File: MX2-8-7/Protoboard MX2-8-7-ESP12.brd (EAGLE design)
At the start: 64.4 x 71.2 mm, 146 parts, among them J1 DCJ0202

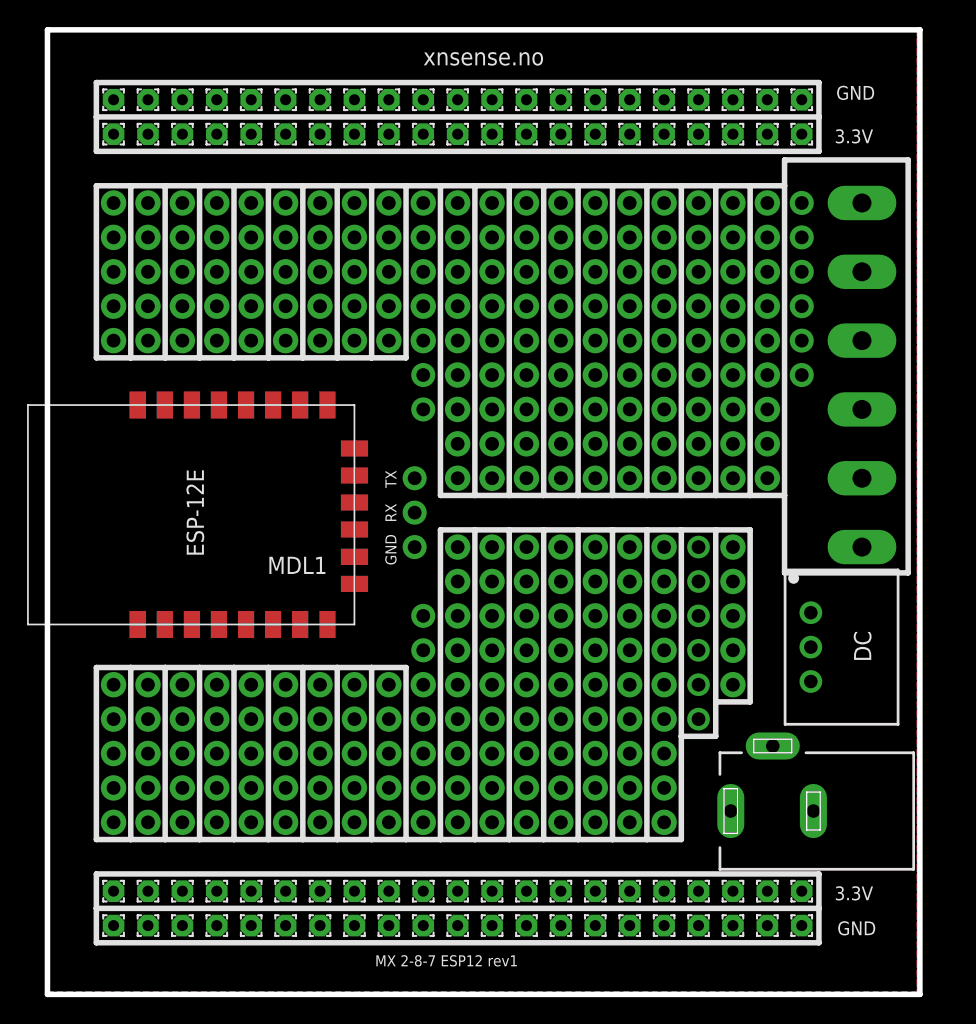
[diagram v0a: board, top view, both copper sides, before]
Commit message: Change usb connector
Change to correct usb connecter and moved esp8266 bit more onto the
board.
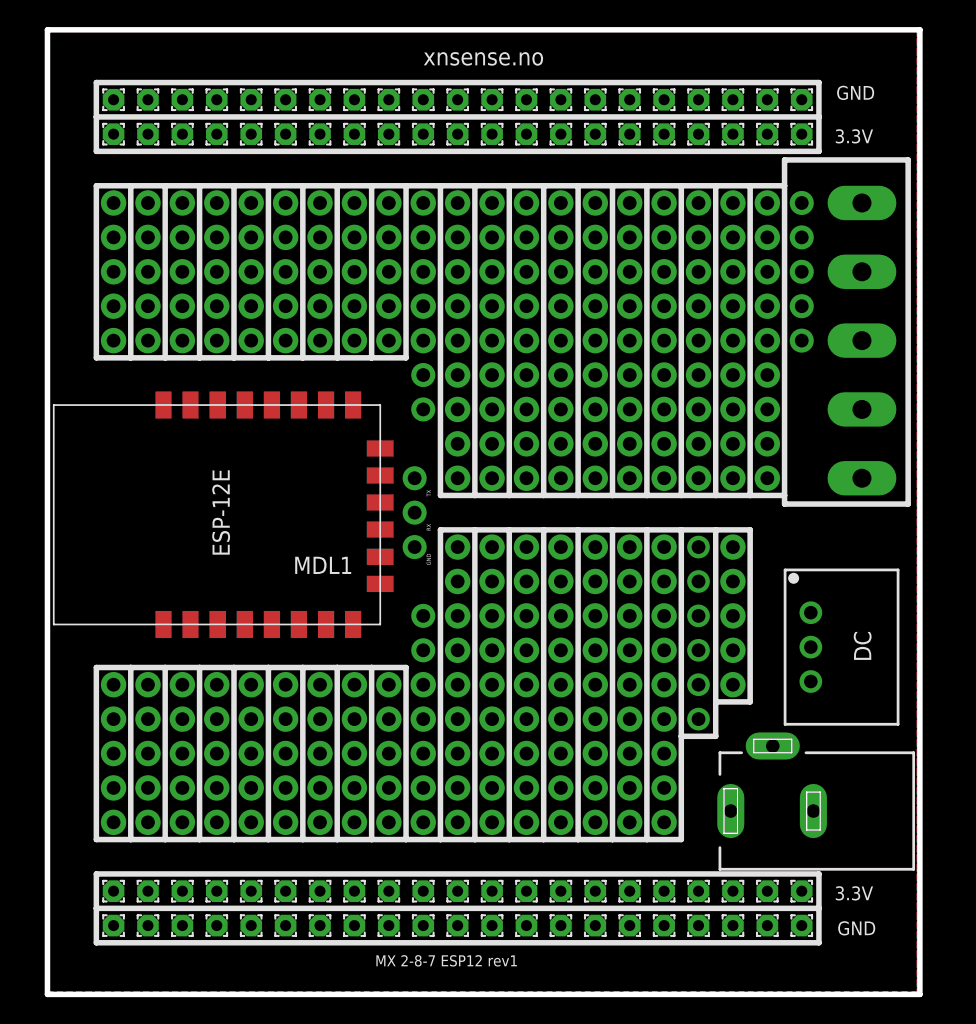
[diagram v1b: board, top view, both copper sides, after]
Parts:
- removed JP11: (no value), adafruit:1X01-CLEANBIG
- removed JP17: (no value), adafruit:1X1-BIGPOGO
- moved MDL1 1.91 mm to (14.6, 34.9)
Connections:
- removed net N$45: JP11.1, JP17.P$1

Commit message: Update esp component and usb
test
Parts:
- removed J1: DCJ0202, con-jack:DCJ0202
- removed MDL1: (no value), ESP8266-ESP12E:ESP8266-ESP12E
- added U2: (no value), SparkFun-PowerIC:SOT23-5
- added X1: ESP-12E, microbuilder:ESP-12E
- added X2: (no value), microbuilder:4UCONN_20329_V2
- moved DC 6.63 mm to (58.5, 19.3), turned to 180 degrees
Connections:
- new net N$45: TX.1, X1.15
- net GND: now also U2.2, X1.9; no longer J1.2, J1.3, MDL1.9
- net N$1: now also X1.14; no longer MDL1.14
- net N$22: now also X1.1; no longer MDL1.1
- net N$23: now also X1.2; no longer MDL1.2
- net N$24: now also X1.3; no longer MDL1.3
- net N$25: now also X1.4; no longer MDL1.4
- net N$26: now also X1.5; no longer MDL1.5
- net N$27: now also X1.6; no longer MDL1.6
- net N$28: now also X1.7; no longer MDL1.7
- net N$3: now also X1.13; no longer MDL1.13
- net N$4: now also X1.12; no longer MDL1.12
- net N$46: now also X1.16; no longer MDL1.15
- net N$47: now also X2.BASE@1, X2.BASE@2, X2.GND, X2.SPRT@1, X2.SPRT@2, X2.SPRT@3, X2.SPRT@4; no longer MDL1.16, TX.1
- net N$5: now also X1.11; no longer MDL1.11
- net N$6: now also X1.10; no longer MDL1.10
- net VCC: now also U2.1, U2.3, X2.VBUS; no longer J1.1
- net VDD: now also U2.5, X1.8; no longer MDL1.8

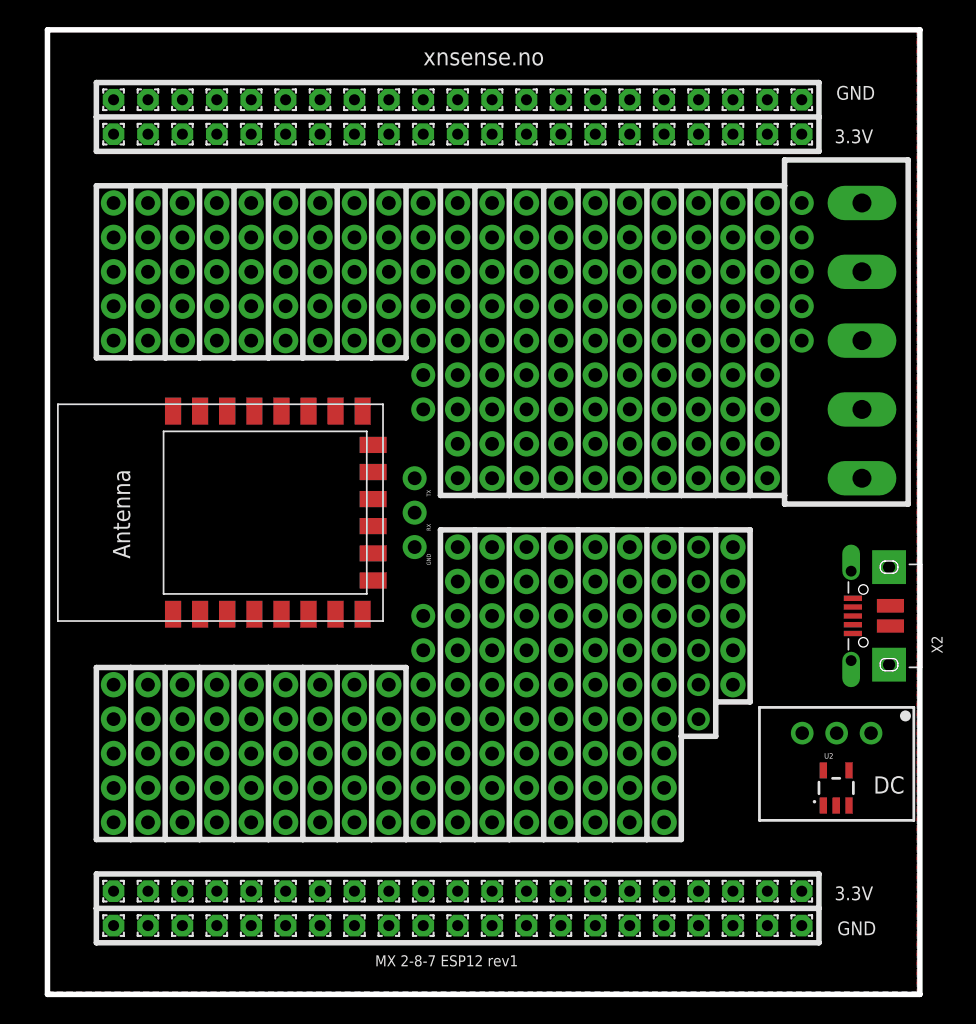
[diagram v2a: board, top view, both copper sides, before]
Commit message: Fixed revert and sccidental deletion
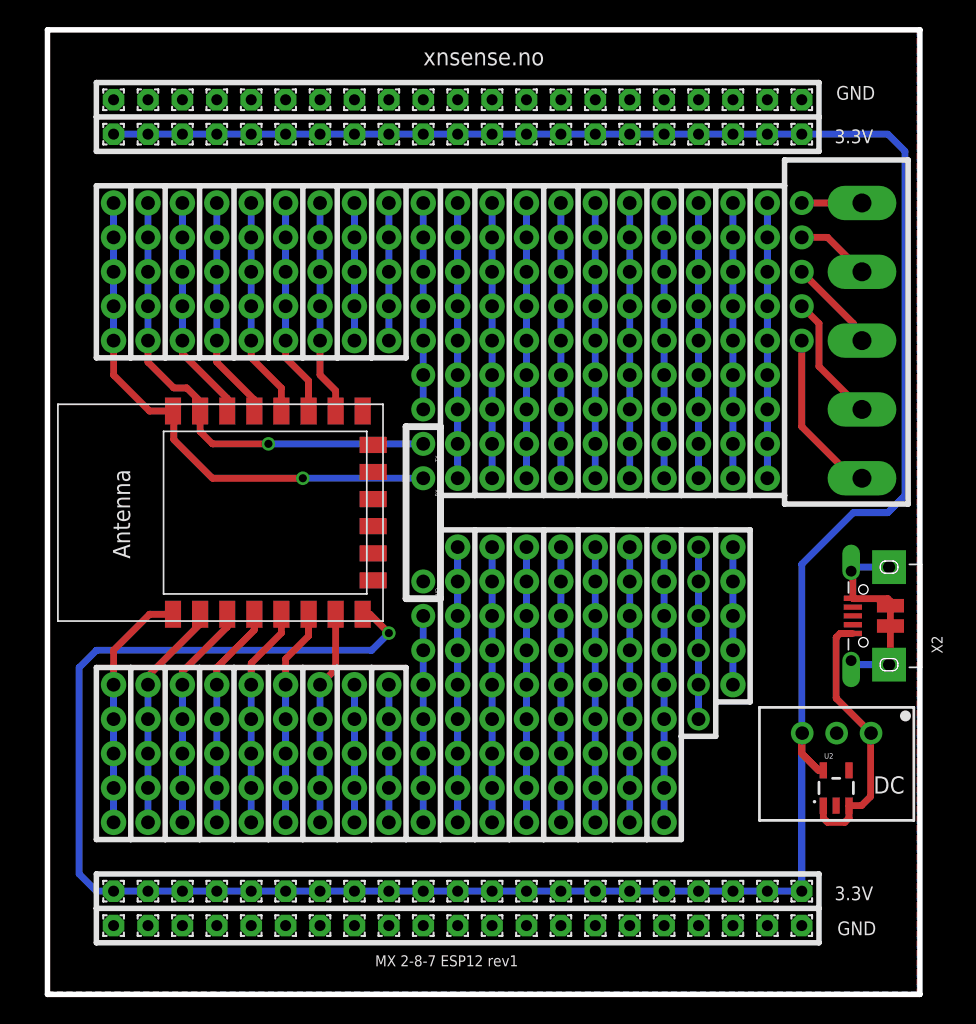
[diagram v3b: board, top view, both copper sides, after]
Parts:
- moved J8 15.2 mm to (5.08, 48.3)
- moved J7 10.2 mm to (7.62, 48.3)
- moved J4 5.08 mm to (17.8, 48.3)
- moved J3 5.08 mm to (15.2, 48.3)
- moved J39 5.08 mm to (10.2, 48.3)
- moved J5 5.08 mm to (20.3, 48.3)
- moved J2 5.08 mm to (12.7, 48.3)
- moved GND 2.62 mm to (27.9, 30.5)
- moved RX 2.62 mm to (27.9, 38.1)
- moved TX 2.62 mm to (27.9, 40.6)
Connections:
- removed net N$7: J7.1, J7.2, J7.3, J7.4, J7.5
- removed net N$8: J8.1, J8.2, J8.3, J8.4, J8.5
- net N$45: now also J7.1, J7.2, J7.3, J7.4, J7.5
- net N$46: now also J8.1, J8.2, J8.3, J8.4, J8.5
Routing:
- net VDD: track 0.00 -> 229.0 mm, vias 0 -> 1
- net N$46: track 0.00 -> 39.9 mm, vias 0 -> 1
- net N$45: track 0.00 -> 35.9 mm, vias 0 -> 1
- net N$39: track 0.00 -> 20.3 mm
- net N$38: track 0.00 -> 20.3 mm
- net N$37: track 0.00 -> 20.3 mm
- net N$36: track 0.00 -> 20.3 mm
- net N$35: track 0.00 -> 20.3 mm
- net N$33: track 0.00 -> 20.3 mm
- net N$32: track 0.00 -> 20.3 mm
- net N$21: track 0.00 -> 20.3 mm
- net N$20: track 0.00 -> 20.3 mm
- net N$19: track 0.00 -> 20.3 mm
- net N$18: track 0.00 -> 20.3 mm
- net N$17: track 0.00 -> 20.3 mm
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
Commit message: Silkscreen text fixes
Silkscreen text fixes
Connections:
- net N$45: now also RX.1; no longer TX.1
- net N$46: now also TX.1; no longer RX.1
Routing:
- net N$46: track 39.9 -> 41.7 mm
- net N$45: track 35.9 -> 36.8 mm
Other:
- board text added: "MX 2-8-7 ESP12 rev 1"
- board text removed: "MX 2-8-7 ESP12 rev1"
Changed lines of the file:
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@@
 <?xml version="1.0" encoding="utf-8"?>
 <!DOCTYPE eagle SYSTEM "eagle.dtd">
-<eagle version="7.6.0">
+<eagle version="7.7.0">
 <drawing>
 <settings>
@@
 <wire x1="46.99" y1="19.05" x2="46.99" y2="34.29" width="0.4064" layer="25"/>
 <wire x1="49.53" y1="34.29" x2="49.53" y2="21.59" width="0.4064" layer="25"/>
-<text x="27.94" y="68.58" size="1.27" layer="25">xnsense.no</text>
-<text x="34.945" y="2.885" size="0.8128" layer="25" rot="R180">MX 2-8-7 ESP12 rev1</text>
+<text x="24.13" y="68.58" size="1.778" layer="25">xnsense.no</text>
+<text x="43.835" y="2.885" size="1.778" layer="25" rot="R180">MX 2-8-7 ESP12 rev 1</text>
 <wire x1="63.735" y1="61.595" x2="54.61" y2="61.595" width="0.4064" layer="25"/>
 <wire x1="54.61" y1="61.595" x2="54.61" y2="59.69" width="0.4064" layer="25"/>
 <wire x1="63.735" y1="61.595" x2="63.735" y2="36.195" width="0.4064" layer="25"/>
-<text x="58.42" y="66.04" size="1.016" layer="25">GND</text>
-<text x="58.5" y="4.37" size="1.016" layer="25">GND</text>
+<text x="58.3" y="66.04" size="1.016" layer="25">GND</text>
+<text x="58.3" y="4.37" size="1.016" layer="25">GND</text>
 <text x="58.3" y="62.83" size="1.016" layer="25">3.3V</text>
 <text x="58.3" y="6.95" size="1.016" layer="25">3.3V</text>
@@
 <attribute name="VALUE" x="53.975" y="21.59" size="1.27" layer="27" rot="R90"/>
 </element>
+<element name="RX" library="adafruit" package="1X01-CLEANBIG" value="" x="27.94" y="38.1" smashed="yes">
+<attribute name="NAME" x="26.2763" y="37.3888" size="0.6096" layer="25" ratio="10" rot="R90"/>
+<attribute name="VALUE" x="26.67" y="34.925" size="1.27" layer="27"/>
+</element>
 <element name="TX" library="adafruit" package="1X01-CLEANBIG" value="" x="27.94" y="40.64" smashed="yes">
-<attribute name="NAME" x="29.1338" y="39.2938" size="0.3048" layer="25" ratio="10" rot="R90"/>
+<attribute name="NAME" x="26.2763" y="39.9288" size="0.6096" layer="25" ratio="10" rot="R90"/>
 <attribute name="VALUE" x="26.67" y="37.465" size="1.27" layer="27"/>
 </element>
-<element name="RX" library="adafruit" package="1X01-CLEANBIG" value="" x="27.94" y="38.1" smashed="yes">
-<attribute name="NAME" x="29.1338" y="36.7538" size="0.3048" layer="25" ratio="10" rot="R90"/>
-<attribute name="VALUE" x="26.67" y="34.925" size="1.27" layer="27"/>
-</element>
 <element name="GND" library="adafruit" package="1X01-CLEANBIG" value="" x="27.94" y="30.48" smashed="yes">
-<attribute name="NAME" x="29.1338" y="29.1338" size="0.3048" layer="25" ratio="10" rot="R90"/>
+<attribute name="NAME" x="26.2763" y="29.4513" size="0.6096" layer="25" ratio="10" rot="R90"/>
 <attribute name="VALUE" x="26.67" y="27.305" size="1.27" layer="27"/>
 </element>
@@
 </signal>
 <signal name="N$46">
-<contactref element="RX" pad="1"/>
+<contactref element="TX" pad="1"/>
 <contactref element="X1" pad="16"/>
 <contactref element="J8" pad="1"/>
@@
 <wire x1="7.74" y1="43.06" x2="5.08" y2="45.72" width="0.508" layer="1"/>
 <wire x1="5.08" y1="45.72" x2="5.08" y2="48.26" width="0.508" layer="1"/>
-<wire x1="27.94" y1="38.1" x2="19.05" y2="38.1" width="0.508" layer="16"/>
-<via x="19.05" y="38.1" extent="1-16" drill="0.6"/>
-<wire x1="19.05" y1="38.1" x2="12.3825" y2="38.1" width="0.508" layer="1"/>
-<wire x1="12.3825" y1="38.1" x2="9.525" y2="40.9575" width="0.508" layer="1"/>
-<wire x1="9.525" y1="40.9575" x2="9.525" y2="43.005" width="0.508" layer="1"/>
+<wire x1="5.08" y1="55.88" x2="5.08" y2="58.42" width="0" layer="19" extent="1-1"/>
+<wire x1="5.08" y1="53.34" x2="5.08" y2="55.88" width="0" layer="19" extent="1-1"/>
+<wire x1="5.08" y1="50.8" x2="5.08" y2="48.26" width="0" layer="19" extent="16-16"/>
+<wire x1="27.94" y1="40.64" x2="15.24" y2="40.64" width="0.508" layer="16"/>
+<wire x1="15.24" y1="40.64" x2="12.7" y2="38.1" width="0.508" layer="16"/>
+<via x="12.7" y="38.1" extent="1-16" drill="0.508"/>
+<wire x1="12.7" y1="38.1" x2="11.1125" y2="38.1" width="0.508" layer="1"/>
+<wire x1="11.1125" y1="38.1" x2="9.525" y2="39.6875" width="0.508" layer="1"/>
+<wire x1="9.525" y1="39.6875" x2="9.525" y2="43.005" width="0.508" layer="1"/>
 <wire x1="9.525" y1="43.005" x2="9.47" y2="43.06" width="0.508" layer="1"/>
-<wire x1="5.08" y1="53.34" x2="5.08" y2="55.88" width="0" layer="19" extent="1-1"/>
-<wire x1="5.08" y1="50.8" x2="5.08" y2="53.34" width="0" layer="19" extent="1-1"/>
-<wire x1="5.08" y1="58.42" x2="5.08" y2="55.88" width="0" layer="19" extent="1-1"/>
 </signal>
 <signal name="N$11">
@@
 <signal name="N$45">
 <contactref element="X1" pad="15"/>
-<contactref element="TX" pad="1"/>
+<contactref element="RX" pad="1"/>
 <contactref element="J7" pad="5"/>
 <contactref element="J7" pad="4"/>
@@
 <wire x1="9.525" y1="44.7675" x2="7.62" y2="46.6725" width="0.508" layer="1"/>
 <wire x1="7.62" y1="46.6725" x2="7.62" y2="48.26" width="0.508" layer="1"/>
-<wire x1="11.47" y1="43.06" x2="11.47" y2="41.5525" width="0.508" layer="1"/>
-<wire x1="11.47" y1="41.5525" x2="12.3825" y2="40.64" width="0.508" layer="1"/>
-<wire x1="12.3825" y1="40.64" x2="16.51" y2="40.64" width="0.508" layer="1"/>
-<via x="16.51" y="40.64" extent="1-16" drill="0.6"/>
-<wire x1="16.51" y1="40.64" x2="27.94" y2="40.64" width="0.508" layer="16"/>
+<wire x1="7.62" y1="55.88" x2="7.62" y2="58.42" width="0" layer="19" extent="1-1"/>
 <wire x1="7.62" y1="53.34" x2="7.62" y2="55.88" width="0" layer="19" extent="1-1"/>
-<wire x1="7.62" y1="50.8" x2="7.62" y2="53.34" width="0" layer="19" extent="1-1"/>
-<wire x1="7.62" y1="58.42" x2="7.62" y2="55.88" width="0" layer="19" extent="1-1"/>
+<wire x1="7.62" y1="50.8" x2="7.62" y2="48.26" width="0" layer="19" extent="16-16"/>
+<wire x1="27.94" y1="38.1" x2="16.51" y2="38.1" width="0.508" layer="16"/>
+<via x="16.51" y="38.1" extent="1-16" drill="0.508"/>
+<wire x1="16.51" y1="38.1" x2="15.24" y2="38.1" width="0.508" layer="1"/>
+<wire x1="15.24" y1="38.1" x2="11.43" y2="41.91" width="0.508" layer="1"/>
+<wire x1="11.43" y1="41.91" x2="11.43" y2="43.02" width="0.508" layer="1"/>
+<wire x1="11.43" y1="43.02" x2="11.47" y2="43.06" width="0.508" layer="1"/>
 </signal>
 <signal name="N$47">
